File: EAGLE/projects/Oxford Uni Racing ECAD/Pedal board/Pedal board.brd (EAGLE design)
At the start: 165.1 x 216.8 mm, 50 parts, among them IC1 AD711N, J1 ASS + BOTS, J2 THR_1_2, J3 PWR_CAN, J6 BR_POS_PRESS_STWH, J7 T821108A1S100CEU, K2 EC2-12TNU, T1 BT169, X2 D-SUB9-H2M09ST

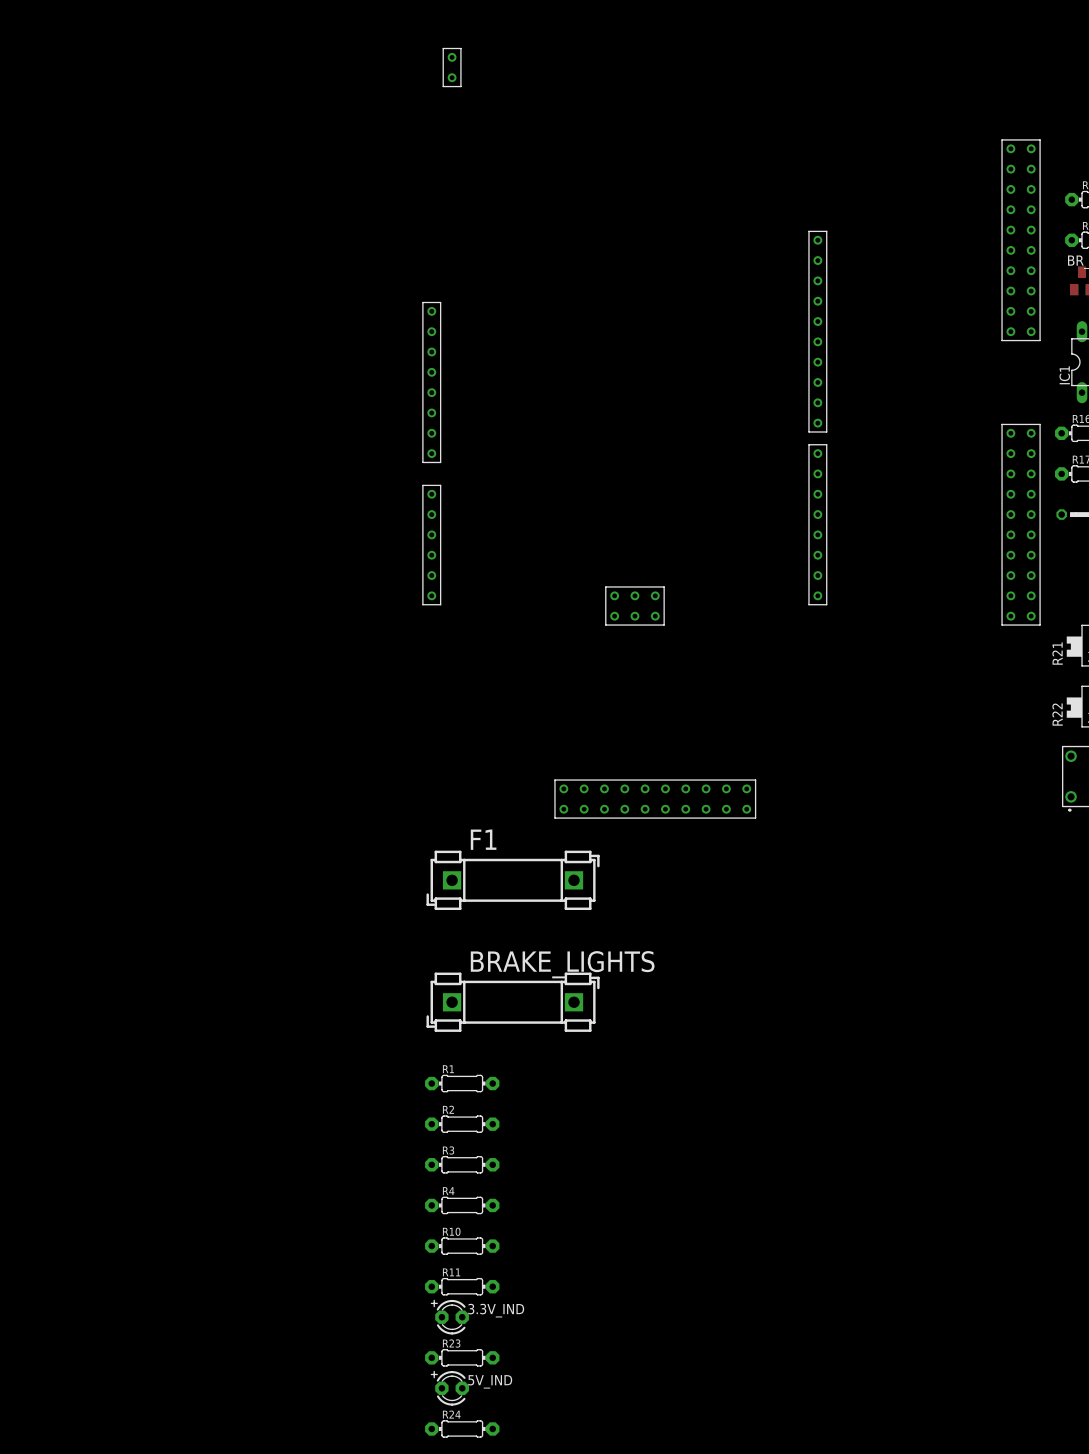
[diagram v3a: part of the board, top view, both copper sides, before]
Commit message: replaced MCUs on pedal and dashboard to not include ext1&2
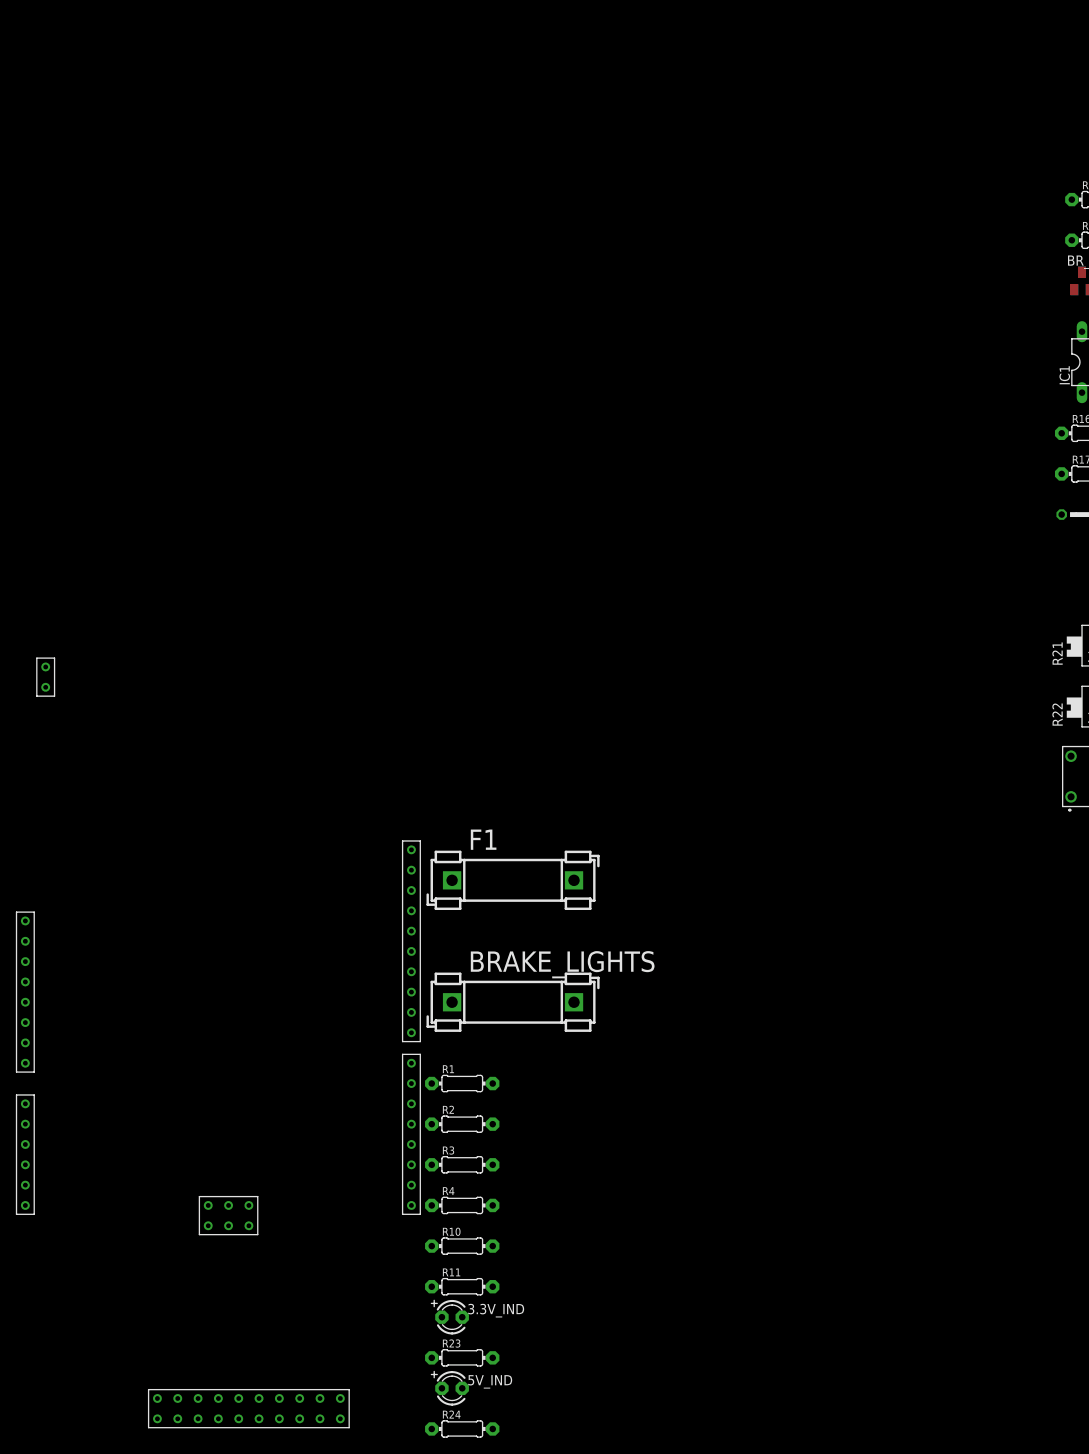
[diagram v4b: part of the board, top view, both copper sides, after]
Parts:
- U$1: value SAMC21-XPLAINED-PRO -> SAMC21-XPLAINED-PRO_NO_EXT1&2; device Oxford Uni Racing Custom Blueprints:SAMC21-XPLAINED-PRO -> Oxford Uni Racing Custom Blueprints:SAMC21-XPLAINED-PRO_NO_EXT1&2
- moved U$1 91.6 mm to (-129.5, -273.1)
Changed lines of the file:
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@@
 <attribute name="VALUE" x="7.62" y="-219.71" size="1.27" layer="27" align="center"/>
 </element>
-<element name="U$1" library="Oxford Uni Racing Custom Blueprints" package="SAMC21-XPLAINED-PRO" value="SAMC21-XPLAINED-PRO" x="-78.74" y="-196.85" smashed="yes"/>
 <element name="F1" library="fuse" library_urn="urn:adsk.eagle:library:233" package="FUSE_HOLDER_5X20MM" package3d_urn="urn:adsk.eagle:package:14079/1" value="1A" x="-76.2" y="-232.41" smashed="yes">
 <attribute name="MF" value="" x="-76.2" y="-232.41" size="1.778" layer="27" display="off"/>
@@
 <attribute name="VALUE" x="-76.5556" y="-301.4726" size="0.9906" layer="27" ratio="12"/>
 </element>
+<element name="U$1" library="Oxford Uni Racing Custom Blueprints" package="SAMC21-XPLAINED-PRO_NO_EXT1&amp;2" value="SAMC21-XPLAINED-PRO_NO_EXT1&amp;2" x="-129.54" y="-273.05" smashed="yes"/>
 </elements>
 <signals>
@@
 <contactref element="C2" pad="2"/>
 <wire x1="7.62" y1="-83.82" x2="10.92835" y2="-83.82" width="0.8128" layer="16"/>
+<contactref element="R24" pad="1"/>
+<contactref element="R23" pad="1"/>
 <contactref element="U$1" pad="J802-5"/>
 <contactref element="U$1" pad="J802-6"/>
-<contactref element="R24" pad="1"/>
-<contactref element="R23" pad="1"/>
-<wire x1="-78.74" y1="-176.53" x2="-78.74" y2="-173.99" width="0" layer="19" extent="1-1"/>
-<wire x1="0" y1="-181.61" x2="-78.74" y2="-176.53" width="0" layer="19" extent="1-1"/>
+<wire x1="18.415" y1="-204.47" x2="18.415" y2="-212.09" width="0" layer="19" extent="1-1"/>
+<wire x1="0" y1="-181.61" x2="18.415" y2="-204.47" width="0" layer="19" extent="1-1"/>
 <wire x1="10.16" y1="-171.45" x2="0" y2="-181.61" width="0" layer="19" extent="1-1"/>
 <wire x1="3.49" y1="-158.58" x2="10.16" y2="-171.45" width="0" layer="19" extent="1-1"/>
 <wire x1="1.27" y1="-152.4" x2="3.49" y2="-158.58" width="0" layer="19" extent="1-1"/>
-<wire x1="18.415" y1="-204.47" x2="0" y2="-181.61" width="0" layer="19" extent="1-1"/>
-<wire x1="18.415" y1="-212.09" x2="18.415" y2="-204.47" width="0" layer="19" extent="1-1"/>
 <wire x1="11.43" y1="-120.65" x2="1.27" y2="-152.4" width="0" layer="19" extent="1-1"/>
 <wire x1="9.62786875" y1="-89.58071875" x2="11.43" y2="-120.65" width="0" layer="19" extent="1-1"/>
@@
 <wire x1="149.86" y1="34.29" x2="134.62" y2="22.86" width="0" layer="19" extent="16-16"/>
 <wire x1="149.86" y1="36.83" x2="149.86" y2="34.29" width="0" layer="19" extent="1-1"/>
-<wire x1="-78.74" y1="-292.1" x2="-78.74" y2="-176.53" width="0" layer="19" extent="1-1"/>
+<wire x1="-78.74" y1="-292.1" x2="18.415" y2="-212.09" width="0" layer="19" extent="1-1"/>
 <wire x1="-78.74" y1="-300.99" x2="-78.74" y2="-292.1" width="0" layer="19" extent="1-1"/>
+<wire x1="-129.54" y1="-252.73" x2="-78.74" y2="-292.1" width="0" layer="19" extent="1-1"/>
+<wire x1="-129.54" y1="-250.19" x2="-129.54" y2="-252.73" width="0" layer="19" extent="1-1"/>
 </signal>
 <signal name="N$7">
@@
 <wire x1="85.21065" y1="8.84555" x2="85.21065" y2="13.97" width="0.6096" layer="16"/>
 <contactref element="U$1" pad="CAN-1"/>
-<wire x1="85.3186" y1="8.7376" x2="-76.2" y2="-129.54" width="0" layer="19" extent="1-1"/>
-<wire x1="85.09" y1="22.86" x2="85.09" y2="20.32" width="0" layer="19" extent="1-1"/>
+<wire x1="85.09" y1="20.32" x2="85.09" y2="22.86" width="0" layer="19" extent="1-1"/>
+<wire x1="-127" y1="-205.74" x2="85.3186" y2="8.7376" width="0" layer="19" extent="1-1"/>
 </signal>
 <signal name="CANH">
@@
 <wire x1="77.47" y1="27.94" x2="77.47" y2="29.21" width="1.27" layer="16"/>
 <contactref element="U$1" pad="CAN-0"/>
-<wire x1="82.55" y1="12.9667" x2="-76.2" y2="-132.08" width="0" layer="19" extent="16-16"/>
+<wire x1="-127" y1="-208.28" x2="83.9343" y2="11.5824" width="0" layer="19" extent="1-1"/>
 </signal>
 <signal name="5V">
@@
 <contactref element="J2" pad="1"/>
 <contactref element="J2" pad="2"/>
-<contactref element="U$1" pad="J802-4"/>
 <contactref element="R21" pad="E"/>
 <contactref element="R10" pad="1"/>
@@
 <contactref element="R1" pad="2"/>
 <contactref element="5V_IND" pad="A"/>
-<wire x1="-71.12" y1="-257.81" x2="-78.74" y2="-171.45" width="0" layer="19" extent="1-1"/>
+<contactref element="U$1" pad="J802-4"/>
+<wire x1="8.89" y1="-118.11" x2="5.715" y2="-204.47" width="0" layer="19" extent="1-1"/>
+<wire x1="-71.12" y1="-257.81" x2="5.715" y2="-204.47" width="0" layer="19" extent="1-1"/>
 <wire x1="-78.74" y1="-262.89" x2="-71.12" y2="-257.81" width="0" layer="19" extent="1-1"/>
 <wire x1="-71.12" y1="-267.97" x2="-78.74" y2="-262.89" width="0" layer="19" extent="1-1"/>
@@
 <wire x1="-78.74" y1="-283.21" x2="-78.74" y2="-278.13" width="0" layer="19" extent="1-1"/>
 <wire x1="-77.47" y1="-295.91" x2="-78.74" y2="-283.21" width="0" layer="19" extent="1-1"/>
-<wire x1="5.715" y1="-204.47" x2="-78.74" y2="-171.45" width="0" layer="19" extent="1-1"/>
-<wire x1="8.89" y1="-118.11" x2="5.715" y2="-204.47" width="0" layer="19" extent="1-1"/>
+<wire x1="-129.54" y1="-247.65" x2="-78.74" y2="-262.89" width="0" layer="19" extent="1-1"/>
 <wire x1="78.3971" y1="11.5824" x2="8.89" y2="-118.11" width="0" layer="19" extent="1-1"/>
 <wire x1="137.16" y1="15.24" x2="78.3971" y2="11.5824" width="0" layer="19" extent="1-1"/>
@@
 <signal name="THR1">
 <contactref element="J2" pad="5"/>
+<contactref element="R1" pad="1"/>
 <contactref element="U$1" pad="J803-0"/>
-<contactref element="R1" pad="1"/>
-<wire x1="-78.74" y1="-184.15" x2="152.4" y2="34.29" width="0" layer="19" extent="1-1"/>
-<wire x1="-78.74" y1="-257.81" x2="-78.74" y2="-184.15" width="0" layer="19" extent="1-1"/>
+<wire x1="-78.74" y1="-257.81" x2="152.4" y2="34.29" width="0" layer="19" extent="1-1"/>
+<wire x1="-129.54" y1="-260.35" x2="-78.74" y2="-257.81" width="0" layer="19" extent="1-1"/>
 </signal>
 <signal name="THR2">
 <contactref element="J2" pad="6"/>
+<contactref element="R2" pad="2"/>
 <contactref element="U$1" pad="J803-1"/>
-<contactref element="R2" pad="2"/>
-<wire x1="-78.74" y1="-186.69" x2="152.4" y2="36.83" width="0" layer="19" extent="1-1"/>
-<wire x1="-71.12" y1="-262.89" x2="-78.74" y2="-186.69" width="0" layer="19" extent="1-1"/>
+<wire x1="-71.12" y1="-262.89" x2="152.4" y2="36.83" width="0" layer="19" extent="1-1"/>
+<wire x1="-129.54" y1="-262.89" x2="-71.12" y2="-262.89" width="0" layer="19" extent="1-1"/>
 </signal>
 <signal name="3.3V">
@@
 <contactref element="R10" pad="2"/>
 <contactref element="U$1" pad="J803-2"/>
-<wire x1="-78.74" y1="-189.23" x2="13.97" y2="-120.65" width="0" layer="19" extent="1-1"/>
-<wire x1="-71.12" y1="-278.13" x2="-78.74" y2="-189.23" width="0" layer="19" extent="1-1"/>
+<wire x1="-71.12" y1="-278.13" x2="-129.54" y2="-265.43" width="0" layer="19" extent="1-1"/>
+<wire x1="13.97" y1="-120.65" x2="-71.12" y2="-278.13" width="0" layer="19" extent="1-1"/>
 </signal>
 <signal name="BRAKE_LIGHTS_OUT">
 <contactref element="R12" pad="1"/>
 <contactref element="U$1" pad="J804-2"/>
-<wire x1="1.27" y1="-147.32" x2="-30.48" y2="-191.77" width="0" layer="19" extent="1-1"/>
+<wire x1="-81.28" y1="-267.97" x2="1.27" y2="-147.32" width="0" layer="19" extent="1-1"/>
 </signal>
 <signal name="N$25">
@@
 <contactref element="U$1" pad="J803-4"/>
 <wire x1="7.62" y1="-181.61" x2="0" y2="-176.53" width="0" layer="19" extent="1-1"/>
-<wire x1="-78.74" y1="-194.31" x2="0" y2="-176.53" width="0" layer="19" extent="1-1"/>
 <wire x1="8.190228125" y1="-68.94195" x2="0" y2="-176.53" width="0" layer="19" extent="16-16"/>
+<wire x1="-129.54" y1="-270.51" x2="0" y2="-176.53" width="0" layer="19" extent="1-1"/>
 </signal>
 <signal name="N$6">
@@
 <contactref element="R4" pad="1"/>
 <contactref element="U$1" pad="J803-3"/>
-<wire x1="-78.74" y1="-191.77" x2="16.51" y2="-120.65" width="0" layer="19" extent="1-1"/>
-<wire x1="-78.74" y1="-273.05" x2="-78.74" y2="-191.77" width="0" layer="19" extent="1-1"/>
+<wire x1="-78.74" y1="-273.05" x2="-129.54" y2="-267.97" width="0" layer="19" extent="1-1"/>
+<wire x1="16.51" y1="-120.65" x2="-78.74" y2="-273.05" width="0" layer="19" extent="1-1"/>
 </signal>
 <signal name="ST_WH_POSS">
 <contactref element="J6" pad="8"/>
+<contactref element="R3" pad="1"/>
 <contactref element="U$1" pad="J803-5"/>
-<contactref element="R3" pad="1"/>
-<wire x1="-78.74" y1="-196.85" x2="16.51" y2="-118.11" width="0" layer="19" extent="1-1"/>
-<wire x1="-78.74" y1="-267.97" x2="-78.74" y2="-196.85" width="0" layer="19" extent="1-1"/>
+<wire x1="-78.74" y1="-267.97" x2="-129.54" y2="-273.05" width="0" layer="19" extent="1-1"/>
+<wire x1="16.51" y1="-118.11" x2="-78.74" y2="-267.97" width="0" layer="19" extent="1-1"/>
 </signal>
 <signal name="12V_BATTERY">

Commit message: added badic pcb layout to pedal board
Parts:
- moved 3.3V_IND 442.4 mm to (148.6, 94.0), turned to 180 degrees
- moved 5V_IND 440.8 mm to (129.5, 94.0), turned to 180 degrees
- moved R23 440.3 mm to (143.5, 90.2)
- moved R24 439.0 mm to (124.5, 90.2)
- moved BRAKE_LIGHTS 381.4 mm to (123.2, 77.5)
- moved U$1 366.2 mm to (63.5, 38.1), flipped to the bottom
- moved F1 363.1 mm to (113.0, 77.5), turned to 90 degrees
- moved R2 357.9 mm to (104.1, 47.0), turned to 180 degrees
- moved R11 356.8 mm to (104.1, 25.4), turned to 180 degrees
- moved R1 350.2 mm to (104.1, 43.2)
- moved R10 342.6 mm to (104.1, 14.0), turned to 180 degrees
- moved R4 341.5 mm to (104.1, 17.8)
- moved R3 340.5 mm to (104.1, 21.6)
- moved K2 302.1 mm to (109.2, 64.8), turned to 180 degrees
- moved R21 300.0 mm to (229.9, 3.81)
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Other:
- board size 165.1 x 216.8 mm -> 165.1 x 114 mm
- board text removed: "Jack Bruford OUR - BOTS Latch"
